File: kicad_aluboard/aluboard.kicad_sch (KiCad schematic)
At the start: 78 parts, among them J1 backplane 2, J2 backplane 1, J3 disp_adlow, J4 disp_adhigh, U1 am2901, U10 am2901, U11 am2901, U2 74LS151, U3 74LS00, U4 74LS00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

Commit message: [aluboard] Fix remarks
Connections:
- net +5V: now also U5.3
- net AOVFL: no longer U5.3
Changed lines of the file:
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@@
 		)
 	)
+	(text_box "v 0.1 BUG: Overflow required aovfh and aovfl. Cut p3 and tie to +5V."
+		(exclude_from_sim no)
+		(at 128.27 274.32 0)
+		(size 27.94 7.62)
+		(margins 0.9525 0.9525 0.9525 0.9525)
+		(stroke
+			(width 0)
+			(type solid)
+		)
+		(fill
+			(type color)
+			(color 255 0 0 1)
+		)
+		(effects
+			(font
+				(size 1.27 1.27)
+			)
+			(justify left top)
+		)
+	)
 	(text_box "ALU Dest"
 		(exclude_from_sim no)
@@
 	)
 	(junction
-		(at 158.75 240.03)
-		(diameter 0)
-		(color 0 0 0 0)
-	)
-	(junction
 		(at 241.3 219.71)
 		(diameter 0)
@@
 	(wire
 		(pts
-			(xy 156.21 240.03) (xy 158.75 240.03)
-		)
-		(stroke
-			(width 0)
-			(type default)
-		)
-	)
-	(wire
-		(pts
 			(xy 369.57 35.56) (xy 372.11 35.56)
 		)
@@
 	(wire
 		(pts
-			(xy 158.75 240.03) (xy 161.29 240.03)
+			(xy 156.21 240.03) (xy 161.29 240.03)
 		)
 		(stroke
@@
 		)
 	)
-	(wire
-		(pts
-			(xy 158.75 266.7) (xy 158.75 240.03)
-		)
-		(stroke
-			(width 0)
-			(type default)
-		)
-	)
 	(bus
 		(pts
@@
 	(wire
 		(pts
-			(xy 154.94 250.19) (xy 161.29 250.19)
+			(xy 153.67 250.19) (xy 161.29 250.19)
 		)
 		(stroke
@@
 	)
 	(label "op8h"
-		(at 154.94 250.19 0)
+		(at 153.67 250.19 0)
 		(effects
 			(font
@@
 					(unit 1)
 				)
+			)
+		)
+	)
+	(symbol
+		(lib_id "power:+5V")
+		(at 158.75 266.7 0)
+		(unit 1)
+		(exclude_from_sim no)
+		(in_bom yes)
+		(on_board yes)
+		(dnp no)
+		(fields_autoplaced yes)
+		(property "Reference" "#PWR033"
+			(at 158.75 270.51 0)
+			(effects
+				(font
+					(size 1.27 1.27)
+				)
+				(hide yes)
+			)
+		)
+		(property "Value" "+5V"
+			(at 158.75 261.62 0)
+			(effects
+				(font
+					(size 1.27 1.27)
+				)
+			)
+		)
+		(property "Footprint" ""
+			(at 158.75 266.7 0)
+			(effects
+				(font
+					(size 1.27 1.27)
+				)
+				(hide yes)
+			)
+		)
+		(property "Datasheet" ""
+			(at 158.75 266.7 0)
+			(effects
+				(font
+					(size 1.27 1.27)
+				)
+				(hide yes)
+			)
+		)
+		(property "Description" "Power symbol creates a global label with name \"+5V\""
+			(at 158.75 266.7 0)
+			(effects
+				(font
+					(size 1.27 1.27)
+				)
+				(hide yes)
+			)
+		)
+		(pin "1"
+		)
+		(instances
+			(project "aluboard"
+				(path "/e866addb-4a2a-480f-b55f-b2ca43a2318b"
+					(reference "#PWR033")
+					(unit 1)
+				)

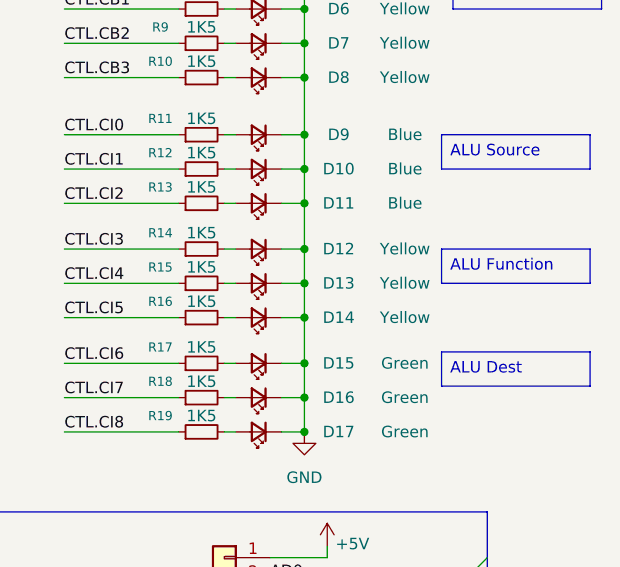
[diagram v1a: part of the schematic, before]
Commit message: [alu] Show flag values.
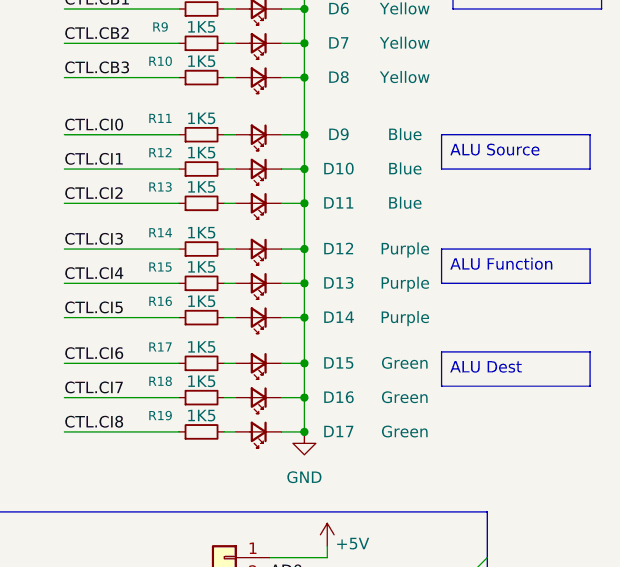
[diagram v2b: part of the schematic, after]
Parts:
- D12, D13, D14: value Yellow -> Purple
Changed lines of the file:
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@@
 			)
 		)
-		(property "Value" "Yellow"
+		(property "Value" "Purple"
 			(at 383.286 66.04 0)
 			(effects
@@
 			)
 		)
-		(property "Value" "Yellow"
+		(property "Value" "Purple"
 			(at 383.286 73.66 0)
 			(effects
@@
 			)
 		)
-		(property "Value" "Yellow"
+		(property "Value" "Purple"
 			(at 383.286 69.85 0)
 			(effects
